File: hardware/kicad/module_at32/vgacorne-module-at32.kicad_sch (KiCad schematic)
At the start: 14 parts, among them J1 to main PCB J4, U1 AT32F405RCT7, Y1 12MHz

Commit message: Add trackpad, mouse column and scroll wheel; move MCU and ports
Layout
- MCU module, USB-C and trackpad move to the right half; the left half
  is now the passive satellite.
- VGA daughterboard bay moves to the inner-back corner so both cables
  leave from the back face. The bay sits 4.5 mm further back than the
  keys need, so both halves are 116 mm deep.
- Azoteq TPS65 trackpad, landscape, right beside Y/H/N under a 1 mm
  overlay. The MCU module moves to a PCB ear behind it, next to the
  VGA bay. trackpad.py selects the pad (TPS65 or 40 mm Cirque); the
  case pocket, J5 connector and QMK driver follow the selection.
- Left half: a mouse column beside T/G/B with a scroll wheel (Bourns
  PEC12R) at the top and left/right-click HE keys beside G and B.

Circuits and firmware
- Mux channels reassigned so the satellite's mouse keys and wheel fill
  its three spare channels. The wheel's A/B contacts are summed into
  four voltage levels on one channel.
- QMK: 44-key LAYOUT and a wheel decoder that feeds QMK's quadrature
  encoder driver. Trackpad on I2C1, with rules.mk now generated. The
  host test covers the wheel.
- libhmk: MS_BTN1/MS_BTN2 on the mouse keys (no encoder support).

Case and renders
- Smoother milled case: 7.25 mm walls, 25 mm minimum outside radius
  and a flat back face at the ports.
- render.py builds Blender Cycles renders from the design geometry.

Co-Authored-By: Claude Opus 5.5 (1M context) <noreply@anthropic.com>
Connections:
- net GND: no longer J1.1 (Pin_1), J1.2 (Pin_2)
- net I2C_SCL: now reaches U1.58 (PB6)
- net I2C_SCL: now also J1.1 (Pin_1)
- net I2C_SDA: now reaches U1.59 (PB7)
- net I2C_SDA: now also J1.2 (Pin_2)
- no-connect marks 38 -> 36

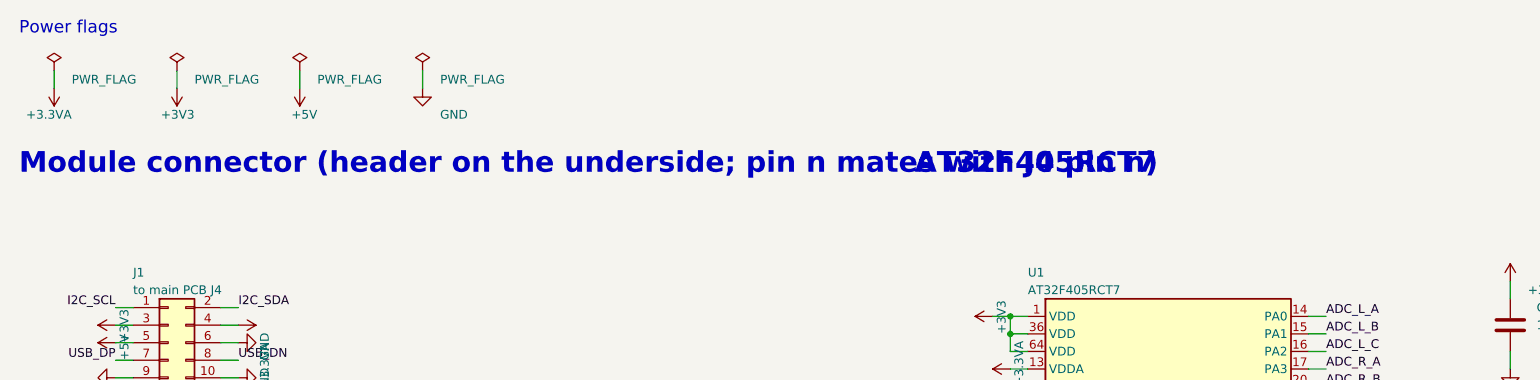
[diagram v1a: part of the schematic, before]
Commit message: Solder the MCU module flat under the trackpad
The plug-in module stood 8 mm tall on a 2x12 socket, on a PCB ear
behind the trackpad that reached back to the rear face. That kept the
right half's back edge straight across most of the trackpad.

It is now a castellated stamp module:
- 19.4 x 25 mm, with 2x12 half-holes at 1.27 mm and every part on top.
- Soldered onto landing pads J4 on the main PCB's tab, beside Y/H/N,
  under the trackpad.
- About 2.7 mm tall: 1.6 mm below the TPS65's well, 2.2 mm below the
  Cirque's.

With the ear gone, a small PCB tongue under the pad carries its FFC
connector J5. The case back now tapers right from the keys; size and
port positions are unchanged.

- New footprints: castellated module edge and matching landing pads.
- Module boards: all parts on top; a label on the flat underside.
- checks.module_connector now compares castellated hole positions with
  landing pad centres.
- Stack-up: module height and clearance are measured against the
  trackpad well.
- Parts can opt out of the BOM (the module's edge pads are not a part).
- Docs, BOM and images regenerated.

Co-Authored-By: Claude Opus 5.5 (1M context) <noreply@anthropic.com>
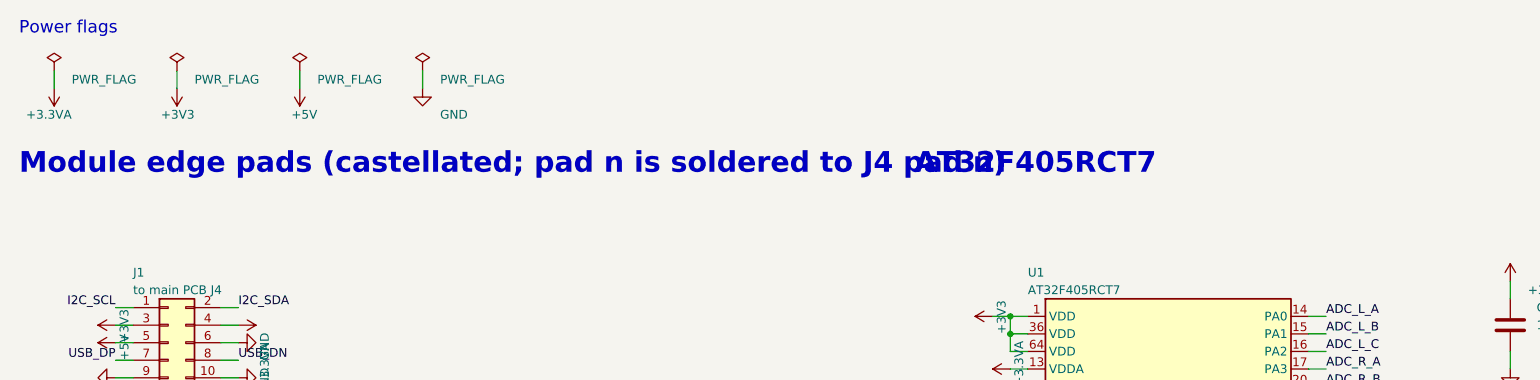
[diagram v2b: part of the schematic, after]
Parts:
- J1: footprint Connector_PinHeader_1.27mm:PinHeader_2x12_P1.27mm_Vertical_SMD -> vgacorne:Module_Castellated_2x12_P1.27mm_19.4x25mm; now left out of the parts list
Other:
- note added: "Module edge pads (castellated; pad n is soldered to J4 pad n)"
- note removed: "Module connector (header on the underside; pin n mates with J4 pin n)"
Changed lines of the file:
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@@
 		(comment 1 "Generated by hardware/generate.py - see docs/architecture.md")
 	)
-	(text "Module connector (header on the underside; pin n mates with J4 pin n)"
+	(text "Module edge pads (castellated; pad n is soldered to J4 pad n)"
 		(exclude_from_sim no)
 		(at 20.32 40.64 0)
@@
 		(unit 1)
 		(exclude_from_sim no)
-		(in_bom yes)
+		(in_bom no)
 		(on_board yes)
 		(dnp no)
@@
 			)
 		)
-		(property "Footprint" "Connector_PinHeader_1.27mm:PinHeader_2x12_P1.27mm_Vertical_SMD"
+		(property "Footprint" "vgacorne:Module_Castellated_2x12_P1.27mm_19.4x25mm"
 			(at 41.91 72.39 0)
 			(effects
@@
 			)
 		)
-		(property "Description" "2x12 1.27 mm header on the underside; mates with J4 on the main PCB"
+		(property "Description" "2x12 castellated edge pads, 1.27 mm; soldered onto J4 on the main PCB (not a part)"
 			(at 41.91 72.39 0)
 			(effects

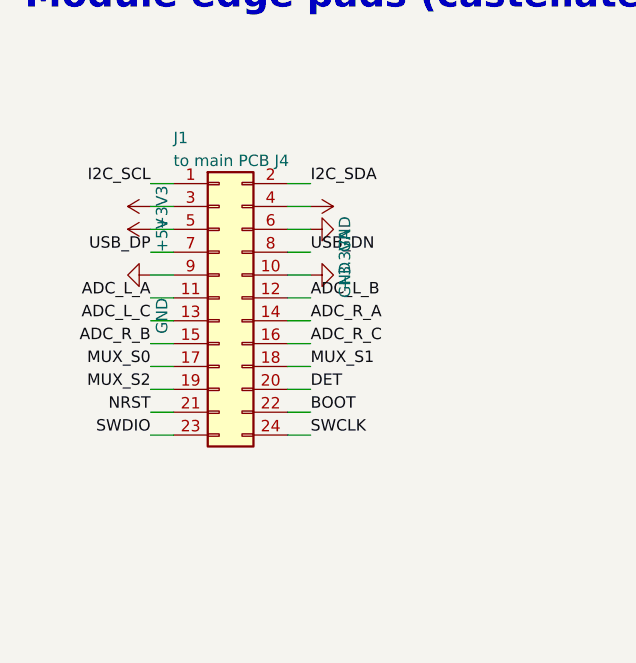
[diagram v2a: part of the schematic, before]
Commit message: Fix design audit findings
Electrical:
- Re-map the castellated module's pads so neighbours on each edge follow
  the LQFP: USB D+/D- together between grounds at the corner nearest the
  USB-C, the six ADC inputs grouped beside +3.3VA, a ground away from the
  select lines.
- Put 1k between each DRV5055 output and its 4.7n cap (TI: no capacitor
  straight on the output).
- STM32F446 module: pull PB2/BOOT1 down so BOOT reaches DFU; pull PA10 up.
- Replace the XC6206 with a second TLV75733, and the link polyfuse with a
  TPS2051C switch (soft start, current limit) so hot-plugging the satellite
  can't brown out the MCU. F1 is now 750 mA.
- USB net class 0.4/0.15 mm: ~97 ohm differential against the pour on both
  2-layer boards (was ~120).
- BOM gains a Tolerance column; part numbers for the F446 crystal.

Mechanical:
- Case foam 2 mm, leaving 0.5 mm under the bottom-side parts (the old stack
  pressed the foam into every sensor).
- USB-C overhangs the ear by 0.46 mm and the opening takes a spec-maximum
  overmould (13.95 x 8.1 mm); the old 11 x 6 mm stopped most plugs short.
- DE-15 rear-mount cutout 20.5 x 11.4 mm; floor pockets under the USB-C and
  encoder pins; plate foam clears the module and the encoder's pins.
- Knob 11.5 mm tall so it clears the encoder's collar.

Docs, PCB images and renders updated to match.

Co-Authored-By: Claude Opus 5.5 (1M context) <noreply@anthropic.com>
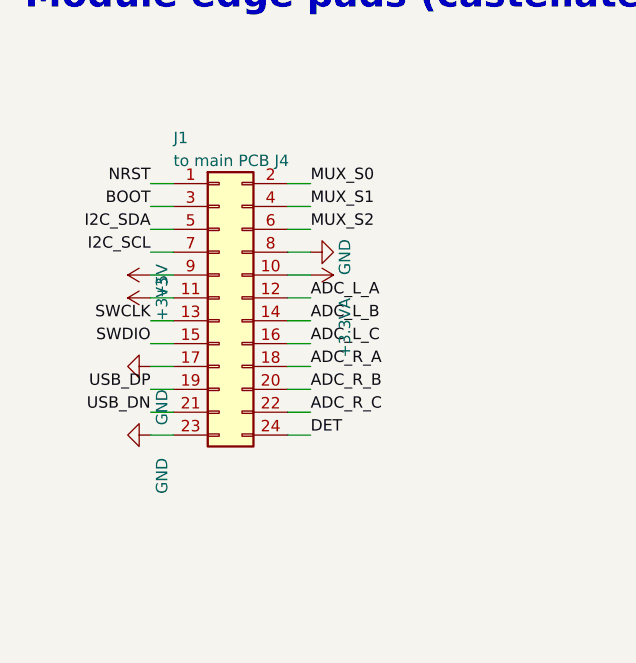
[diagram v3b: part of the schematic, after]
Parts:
- R1: Tolerance (none) -> 1%
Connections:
- net +3.3VA: now also J1.10 (Pin_10); no longer J1.4 (Pin_4)
- net +3V3: now also J1.11 (Pin_11); no longer J1.3 (Pin_3)
- net +5V: now also J1.9 (Pin_9); no longer J1.5 (Pin_5)
- net ADC_L_A: now also J1.12 (Pin_12); no longer J1.11 (Pin_11)
- net ADC_L_B: now also J1.14 (Pin_14); no longer J1.12 (Pin_12)
- net ADC_L_C: now also J1.16 (Pin_16); no longer J1.13 (Pin_13)
- net ADC_R_A: now also J1.18 (Pin_18); no longer J1.14 (Pin_14)
- net ADC_R_B: now also J1.20 (Pin_20); no longer J1.15 (Pin_15)
- net ADC_R_C: now also J1.22 (Pin_22); no longer J1.16 (Pin_16)
- net BOOT: now also J1.3 (Pin_3); no longer J1.22 (Pin_22)
- net DET: now also J1.24 (Pin_24); no longer J1.20 (Pin_20)
- net GND: now also J1.17 (Pin_17), J1.23 (Pin_23), J1.8 (Pin_8); no longer J1.10 (Pin_10), J1.6 (Pin_6), J1.9 (Pin_9)
- net I2C_SCL: now also J1.7 (Pin_7); no longer J1.1 (Pin_1)
- net I2C_SDA: now also J1.5 (Pin_5); no longer J1.2 (Pin_2)
- net MUX_S0: now also J1.2 (Pin_2); no longer J1.17 (Pin_17)
- net MUX_S1: now also J1.4 (Pin_4); no longer J1.18 (Pin_18)
- net MUX_S2: now also J1.6 (Pin_6); no longer J1.19 (Pin_19)
- net NRST: now also J1.1 (Pin_1); no longer J1.21 (Pin_21)
- net SWCLK: now also J1.13 (Pin_13); no longer J1.24 (Pin_24)
- net SWDIO: now also J1.15 (Pin_15); no longer J1.23 (Pin_23)
- net USB_DN: now also J1.21 (Pin_21); no longer J1.8 (Pin_8)
- net USB_DP: now also J1.19 (Pin_19); no longer J1.7 (Pin_7)

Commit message: Add JLC fab outputs; switch the HSE crystals to 12 pF load
`generate.py fab` writes each board's JLCPCB files into hardware/fab/
(git-ignored): a Gerber and drill zip with JLC's KiCad settings, and a BOM
and placement file for the parts with an LCSC number. The numbers live in
vgacorne/fab.py, checked against JLC's library on 2026-10-01; the step
lists the parts without one, which are the hand-fitted ones (J4/J5, ENC1,
the daughterboard's socket and pigtail).

The 20 pF-load crystals with 30 pF caps came to gm_crit ~0.96 mA/V
(AN2867), against the STM32F446's 1 mA/V limit, and the caps were outside
the MCUs' 5-25 pF range. Both modules now use YXC's 12 pF versions
(X32258MOB4SI, X322512MOB4SI) with 15 pF caps: ~0.44 mA/V.

Co-Authored-By: Claude Opus 5.5 (1M context) <noreply@anthropic.com>
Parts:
- C7, C8: value 30p -> 15p
- Y1: MPN X322512MSB4SI -> X322512MOB4SI
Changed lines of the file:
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@@
 			)
 		)
-		(property "Description" "12 MHz, CL 20 pF (libhmk's AT32 port requires 12 MHz)"
+		(property "Description" "12 MHz, CL 12 pF (libhmk's AT32 port requires 12 MHz)"
 			(at 369.57 62.23 0)
 			(effects
@@
 			)
 		)
-		(property "MPN" "X322512MSB4SI"
+		(property "MPN" "X322512MOB4SI"
 			(at 369.57 62.23 0)
 			(effects
@@
 			)
 		)
-		(property "Value" "30p"
+		(property "Value" "15p"
 			(at 161.29 189.23 0)
 			(effects
@@
 			)
 		)
-		(property "Value" "30p"
+		(property "Value" "15p"
 			(at 181.61 189.23 0)
 			(effects
